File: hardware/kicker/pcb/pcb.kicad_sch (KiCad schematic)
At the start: 35 parts, among them J1 Conn_01x04, J2 Conn_01x04, J3 Conn_01x02, Q1 NMOS, U1 XL6019E1, U2 TS4535TP 250GF 009, U4 TC4427AEOA713_C5804606

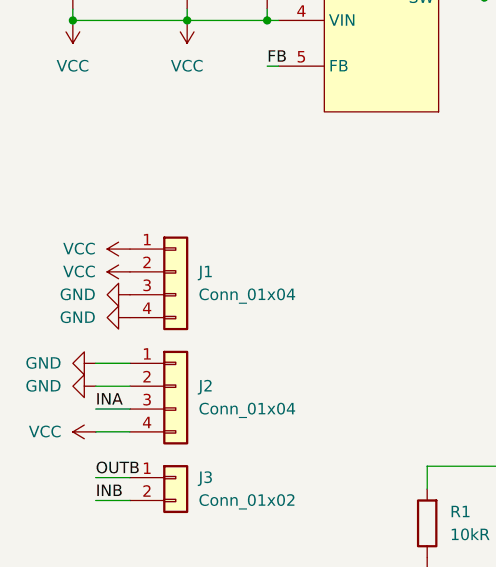
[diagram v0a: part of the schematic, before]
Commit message: fixed non convention following of kicker pcb
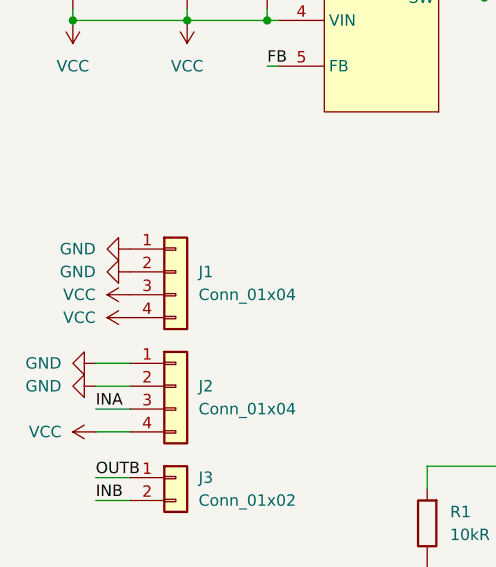
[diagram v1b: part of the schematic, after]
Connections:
- net GND: now also J1.1 (Pin_1), J1.2 (Pin_2); no longer J1.3 (Pin_3), J1.4 (Pin_4)
- net VCC: now also J1.3 (Pin_3), J1.4 (Pin_4); no longer J1.1 (Pin_1), J1.2 (Pin_2)

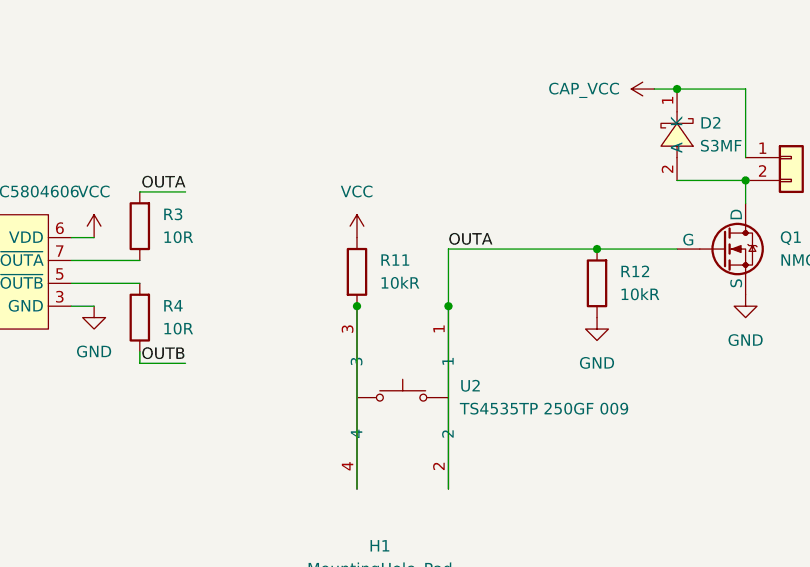
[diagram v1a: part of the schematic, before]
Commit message: changed res value on kicker pcb
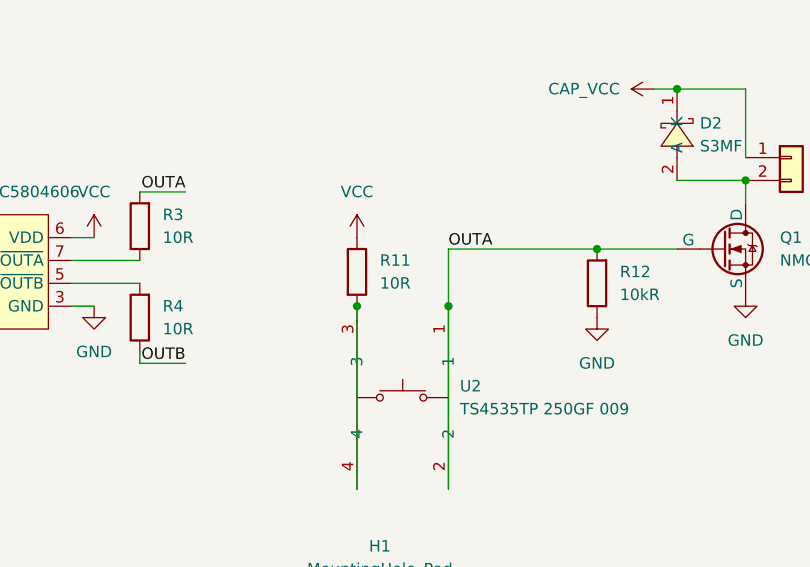
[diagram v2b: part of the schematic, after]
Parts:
- R11: value 10kR -> 10R
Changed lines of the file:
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@@
 	(label "INA"
 		(at 54.61 87.63 0)
-		(fields_autoplaced yes)
 		(effects
 			(font
@@
 	(label "OUTB"
 		(at 54.61 95.25 0)
-		(fields_autoplaced yes)
 		(effects
 			(font
@@
 	(label "OUTA"
 		(at 172.72 92.71 0)
-		(fields_autoplaced yes)
 		(effects
 			(font
@@
 	(label "OUTA"
 		(at 143.51 86.36 180)
-		(fields_autoplaced yes)
 		(effects
 			(font
@@
 	(label "INB"
 		(at 104.14 96.52 0)
-		(fields_autoplaced yes)
 		(effects
 			(font
@@
 	(label "OUTB"
 		(at 143.51 105.41 180)
-		(fields_autoplaced yes)
 		(effects
 			(font
@@
 	(label "FB"
 		(at 113.03 53.34 0)
-		(fields_autoplaced yes)
 		(effects
 			(font
@@
 	(label "INB"
 		(at 54.61 97.79 0)
-		(fields_autoplaced yes)
 		(effects
 			(font
@@
 	(label "INA"
 		(at 104.14 93.98 0)
-		(fields_autoplaced yes)
 		(effects
 			(font
@@
 	(label "FB"
 		(at 73.66 49.53 0)
-		(fields_autoplaced yes)
 		(effects
 			(font
@@
 			)
 		)
-		(property "Value" "10kR"
+		(property "Value" "10R"
 			(at 165.1 96.5199 0)
 			(effects

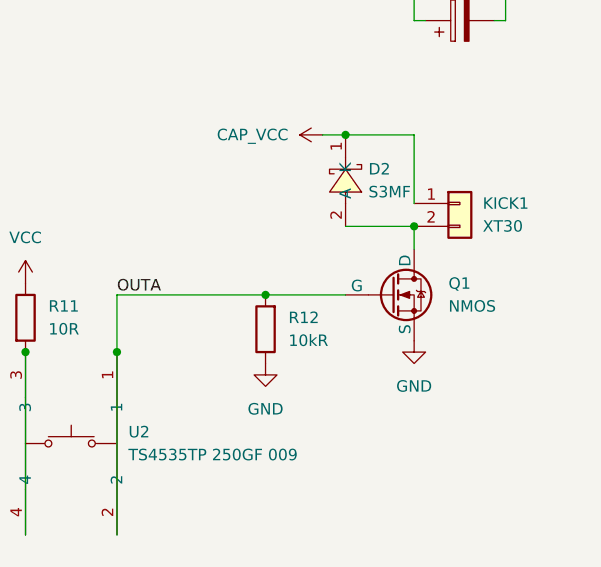
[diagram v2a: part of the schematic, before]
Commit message: corrected mosfet pinout on kicker pcb (will reorder)
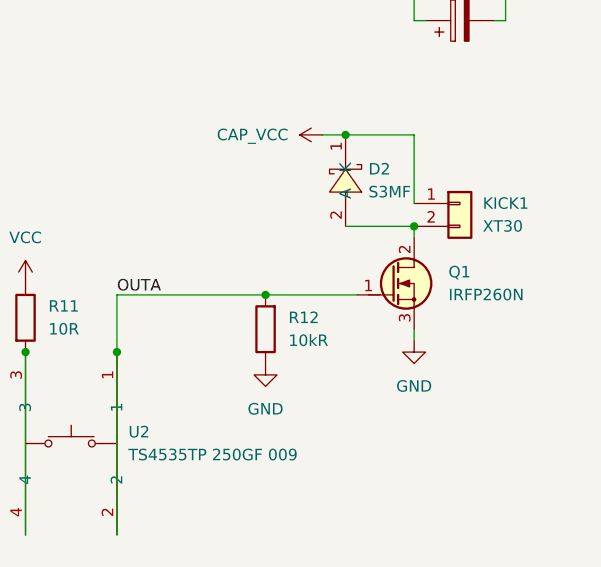
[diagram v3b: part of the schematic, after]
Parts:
- removed Q1: NMOS, Package_TO_SOT_THT:TO-247-3_Vertical, symbol Simulation_SPICE:NMOS
- added Q1: IRFP260N, PCM_Package_TO_SOT_THT_AKL:TO-247-3_Vertical_GDS, symbol PCM_Transistor_MOSFET_AKL:IRFP260N
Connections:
- net GND: now also Q1.3 (S)
- net OUTA: now also Q1.1 (G)
- net at D2.2 (A), KICK1.2 (Pin_2): now also Q1.2 (D)
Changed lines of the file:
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@@
 	(wire
 		(pts
-			(xy 189.23 92.71) (xy 198.12 92.71)
+			(xy 189.23 92.71) (xy 199.39 92.71)
 		)
 		(stroke
@@
 	(wire
 		(pts
+			(xy 205.74 96.52) (xy 205.74 97.79)
+		)
+		(stroke
+			(width 0)
+			(type default)
+		)
+	)
+	(wire
+		(pts
 			(xy 165.1 44.45) (xy 165.1 49.53)
 		)
@@
 	(wire
 		(pts
-			(xy 205.74 85.09) (xy 205.74 87.63)
+			(xy 205.74 85.09) (xy 205.74 86.36)
 		)
 		(stroke
@@
 	)
 	(symbol
+		(lib_id "PCM_Transistor_MOSFET_AKL:IRFP260N")
+		(at 203.2 91.44 0)
+		(unit 1)
+		(exclude_from_sim no)
+		(in_bom yes)
+		(on_board yes)
+		(dnp no)
+		(fields_autoplaced yes)
+		(property "Reference" "Q1"
+			(at 209.55 90.1699 0)
+			(effects
+				(font
+					(size 1.27 1.27)
+				)
+				(justify left)
+			)
+		)
+		(property "Value" "IRFP260N"
+			(at 209.55 92.7099 0)
+			(effects
+				(font
+					(size 1.27 1.27)
+				)
+				(justify left)
+			)
+		)
+		(property "Footprint" "PCM_Package_TO_SOT_THT_AKL:TO-247-3_Vertical_GDS"
+			(at 208.28 88.9 0)
+			(effects
+				(font
+					(size 1.27 1.27)
+				)
+				(hide yes)
+			)
+		)
+		(property "Datasheet" "https://www.tme.eu/Document/385e20890408feac26a85badd08ded6a/irfp260n.pdf"
+			(at 203.2 91.44 0)
+			(effects
+				(font
+					(size 1.27 1.27)
+				)
+				(hide yes)
+			)
+		)
+		(property "Description" "TO-247 N-MOSFET enchancement mode transistor, 200V, 50A, 300W, Alternate KiCAD Library"
+			(at 203.2 91.44 0)
+			(effects
+				(font
+					(size 1.27 1.27)
+				)
+				(hide yes)
+			)
+		)
+		(pin "3"
+		)
+		(pin "2"
+		)
+		(pin "1"
+		)
+		(instances
+			(project "pcb"
+				(path "/5f5875f2-58ee-4f0f-8448-9d85b3ed3f89"
+					(reference "Q1")
+					(unit 1)
+				)
+			)
+		)
+	)
+	(symbol
 		(lib_id "power:VCC")
 		(at 58.42 77.47 90)
@@
 					(unit 1)
 				)
-			)
-		)
-	)
-	(symbol
-		(lib_id "Simulation_SPICE:NMOS")
-		(at 203.2 92.71 0)
-		(unit 1)
-		(exclude_from_sim no)
-		(in_bom yes)
-		(on_board yes)
-		(dnp no)
-		(fields_autoplaced yes)
-		(property "Reference" "Q1"
-			(at 209.55 91.4399 0)
-			(effects
-				(font
-					(size 1.27 1.27)
-				)
-				(justify left)
-			)
-		)
-		(property "Value" "NMOS"
-			(at 209.55 93.9799 0)
-			(effects
-				(font
-					(size 1.27 1.27)
-				)
-				(justify left)
-			)
-		)
-		(property "Footprint" "Package_TO_SOT_THT:TO-247-3_Vertical"
-			(at 208.28 90.17 0)
-			(effects
-				(font
-					(size 1.27 1.27)
-				)
-				(hide yes)
-			)
-		)
-		(property "Datasheet" "https://ngspice.sourceforge.io/docs/ngspice-html-manual/manual.xhtml#cha_MOSFETs"
-			(at 203.2 105.41 0)
-			(effects
-				(font
-					(size 1.27 1.27)
-				)
-				(hide yes)
-			)
-		)
-		(property "Description" "N-MOSFET transistor, drain/source/gate"
-			(at 203.2 92.71 0)
-			(effects
-				(font
-					(size 1.27 1.27)
-				)
-				(hide yes)
-			)
-		)
-		(property "Sim.Device" "NMOS"
-			(at 203.2 109.855 0)
-			(effects
-				(font
-					(size 1.27 1.27)
-				)
-				(hide yes)
-			)
-		)
-		(property "Sim.Type" "VDMOS"
-			(at 203.2 111.76 0)
-			(effects
-				(font
-					(size 1.27 1.27)
-				)
-				(hide yes)
-			)
-		)
-		(property "Sim.Pins" "1=D 2=G 3=S"
-			(at 203.2 107.95 0)
-			(effects
-				(font
-					(size 1.27 1.27)
-				)
-				(hide yes)
-			)
-		)
-		(pin "2"
-		)
-		(pin "1"
-		)
-		(pin "3"
-		)
-		(instances
-			(project ""
-				(path "/5f5875f2-58ee-4f0f-8448-9d85b3ed3f89"
-					(reference "Q1")
-					(unit 1)
-				)
